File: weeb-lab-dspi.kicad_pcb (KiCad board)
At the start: 2 copper layers, 35.6 x 58.4 mm, 11 parts, among them J1 SPDIF, J2 MONO RCA, U1 XIAO-RP2350-SMD

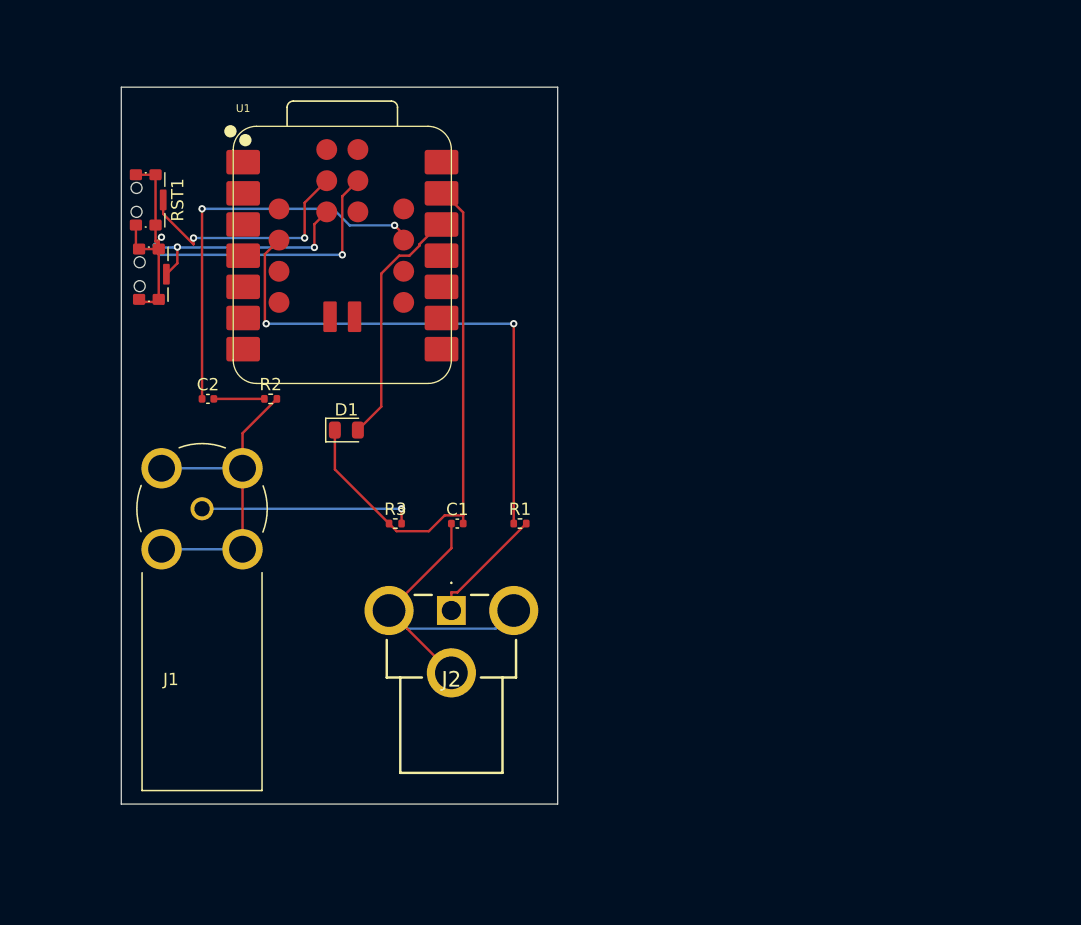
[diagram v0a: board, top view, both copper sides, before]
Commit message: Routed PCB and added more parts
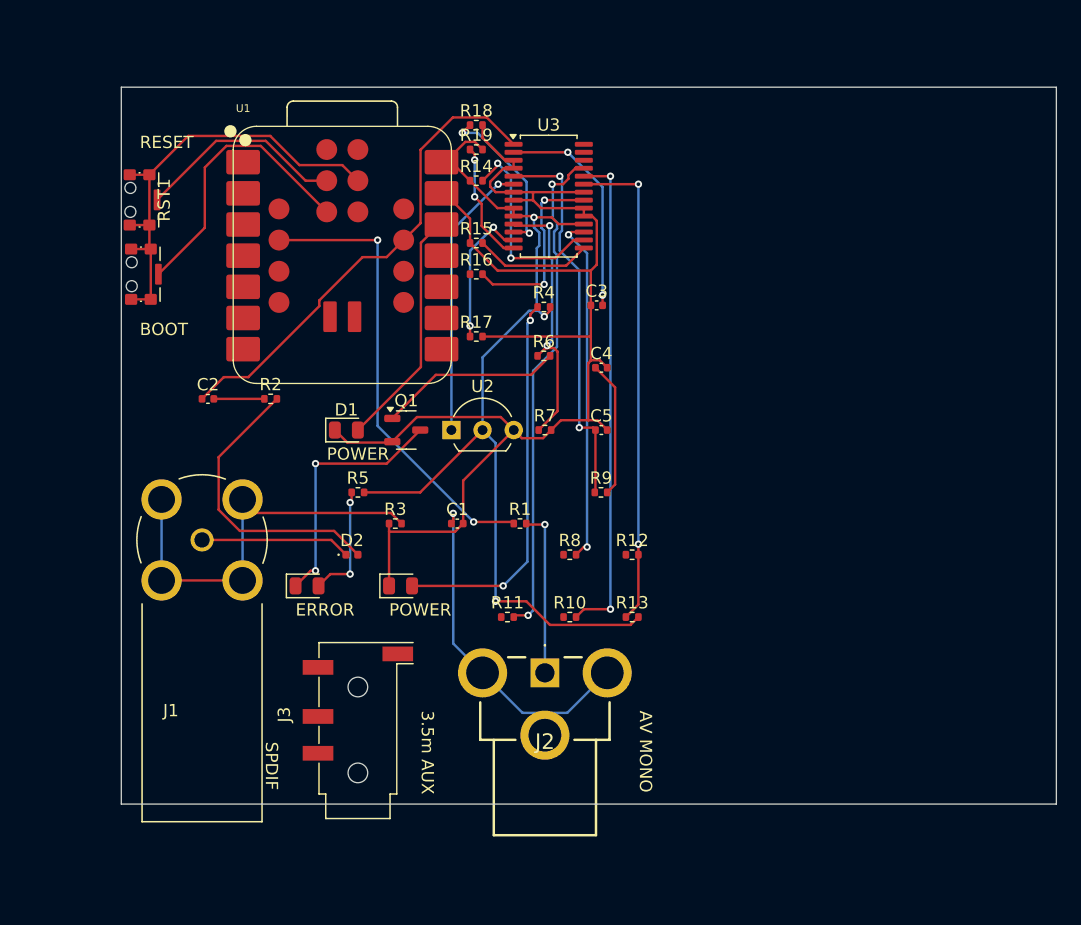
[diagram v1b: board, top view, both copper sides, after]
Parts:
- added C3: 10nf, Capacitor_SMD:C_0402_1005Metric, F.Cu at (176.9, 66.0)
- added C4: 22nf, Capacitor_SMD:C_0402_1005Metric, F.Cu at (177.3, 71.1)
- added C5: 1nf, Capacitor_SMD:C_0402_1005Metric, F.Cu at (177.3, 76.2)
- added D2: BACKFEED_PREVENT, Diode_SMD:D_0402_1005Metric, F.Cu at (157.0, 86.4)
- added D3: POWER, LED_SMD:LED_0805_2012Metric, F.Cu at (161.0, 88.9)
- added D4: ERROR, LED_SMD:LED_0805_2012Metric, F.Cu at (153.3, 88.9)
- added J3: AudioJack3_Ground, Connector_Audio:Jack_3.5mm_KoreanHropartsElec_PJ-320D-4A_Horizontal, F.Cu at (157.5, 99.4)
- added Q1: BC846, Package_TO_SOT_SMD:SOT-23-3, F.Cu at (161.4, 76.2)
- added R10: 33R, Resistor_SMD:R_0402_1005Metric, F.Cu at (174.8, 91.4)
- added R11: 33R, Resistor_SMD:R_0402_1005Metric, F.Cu at (169.7, 91.4)
- added R12: 33R, Resistor_SMD:R_0402_1005Metric, F.Cu at (179.8, 86.4)
- added R13: 47k, Resistor_SMD:R_0402_1005Metric, F.Cu at (179.8, 91.4)
- added R14: 47k, Resistor_SMD:R_0402_1005Metric, F.Cu at (167.1, 55.9)
- added R15: 47k, Resistor_SMD:R_0402_1005Metric, F.Cu at (167.1, 61.0)
- added R16: 33R, Resistor_SMD:R_0402_1005Metric, F.Cu at (167.1, 63.5)
- added R17: 47k, Resistor_SMD:R_0402_1005Metric, F.Cu at (167.1, 68.6)
- added R18: 47k, Resistor_SMD:R_0402_1005Metric, F.Cu at (167.1, 51.4)
- added R19: 47k, Resistor_SMD:R_0402_1005Metric, F.Cu at (167.1, 53.3)
- added R4: 1k2, Resistor_SMD:R_0402_1005Metric, F.Cu at (172.6, 66.2)
- added R5: 1k2, Resistor_SMD:R_0402_1005Metric, F.Cu at (157.5, 81.3)
- added R6: 47k, Resistor_SMD:R_0402_1005Metric, F.Cu at (172.6, 70.2)
- added R7: 47k, Resistor_SMD:R_0402_1005Metric, F.Cu at (172.7, 76.2)
- added R8: 47k, Resistor_SMD:R_0402_1005Metric, F.Cu at (174.8, 86.4)
- added R9: 3k, Resistor_SMD:R_0402_1005Metric, F.Cu at (177.3, 81.3)
- added U2: MCP130-xxxDxTO, Package_TO_SOT_THT:TO-92L_Inline_Wide, F.Cu at (165.1, 76.2)
- added U3: CS8416-xNZ, Package_SO:TSSOP-28_4.4x9.7mm_P0.65mm, F.Cu at (173.0, 57.1)
- moved J2 9.16 mm to (172.7, 96.0)
- moved J1 2.54 mm to (144.8, 85.2)
- moved BOOT1 0.65 mm to (139.8, 63.5)
- moved RST1 0.50 mm to (139.7, 57.4)
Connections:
- net Net-(D1-K) renamed GND
- J1 pad 1: Net-(J1-Pad1) -> Net-(D2-K)
- R2 pad 2: ~ -> Net-(D2-A)
- R3 pad 2: Net-(J1-Pad1) -> ~
- U1 pad 14: unconnected-(U1-5V-Pad14) -> Net-(U1-5V)
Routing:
- net Net-(U1-5V): track 0.00 -> 78.3 mm, vias 0 -> 3
- net GND: track 44.0 -> 112.8 mm
- net Net-(U3-OLRCK): track 0.00 -> 41.0 mm, vias 0 -> 2
- net Net-(U3-OSCLK): track 0.00 -> 40.5 mm, vias 0 -> 2
- net Net-(U3-SDOUT): track 0.00 -> 40.1 mm, vias 0 -> 2
- net Net-(U3-FILT): track 0.00 -> 31.6 mm, vias 0 -> 2
- net Net-(D3-A): track 0.00 -> 31.3 mm, vias 0 -> 2
- net Net-(U3-TX/GPO0): track 0.00 -> 28.6 mm, vias 0 -> 2
- net Net-(D2-A): track 0.00 -> 23.9 mm
- net Net-(U2-~{RST}): track 0.00 -> 22.9 mm, vias 0 -> 1
- net Net-(U3-AD0/~{CS}/NV/RERR): track 0.00 -> 22.3 mm, vias 0 -> 2
- net Net-(D4-K): track 0.00 -> 20.5 mm, vias 0 -> 2
- net Net-(U3-RXN): track 0.00 -> 18.1 mm, vias 0 -> 2
- net Net-(J1-Pad1): track 17.5 -> 0.00 mm, vias 1 -> 0
- net Net-(U3-C/GPO1): track 0.00 -> 16.6 mm, vias 0 -> 2
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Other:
- board size 35.6 x 58.4 mm -> 76.2 x 58.4 mm
- board text added: "3.5m AUX"
- board text added: "AV MONO"
- board text added: "BOOT"
- board text added: "ERROR"
- board text added: "POWER"
- board text added: "RESET"
- board text added: "SPDIF"

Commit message: Almost  Complete
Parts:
- removed J3: AudioJack3_Ground, Connector_Audio:Jack_3.5mm_KoreanHropartsElec_PJ-320D-4A_Horizontal
- added C10: 0.1uf, Capacitor_SMD:C_0402_1005Metric, F.Cu at (165.5, 99.1)
- added C11: 0.1uf, Capacitor_SMD:C_0402_1005Metric, F.Cu at (170.6, 99.1)
- added C12: 10uf, Capacitor_SMD:C_0402_1005Metric, F.Cu at (163.0, 99.1)
- added C13: 10uf, Capacitor_SMD:C_0402_1005Metric, F.Cu at (163.0, 101.0)
- added C6: 10uf, Capacitor_SMD:C_0402_1005Metric, F.Cu at (177.8, 83.8)
- added C7: 10uf, Capacitor_SMD:C_0402_1005Metric, F.Cu at (144.8, 68.6)
- added C8: 10uf, Capacitor_SMD:C_0402_1005Metric, F.Cu at (175.3, 83.8)
- added C9: 10uf, Capacitor_SMD:C_0402_1005Metric, F.Cu at (144.8, 66.0)
- added D5: BACKFEED_PREVENT, Diode_SMD:D_0402_1005Metric, F.Cu at (174.8, 53.3)
- added J4: AudioJack3_Ground, Connector_Audio:Jack_3.5mm_CUI_SJ-3524-SMT_Horizontal, F.Cu at (156.7, 103.6)
- added LEFT1: TPA6203A1DRB, Package_DFN_QFN:Texas_DRB0008A, F.Cu at (166.6, 103.2)
- added RIGHT1: TPA6203A1DRB, Package_DFN_QFN:Texas_DRB0008A, F.Cu at (171.4, 103.2)
- added U4: CS434x-xZZ, Package_SO:TSSOP-10_3x3mm_P0.5mm, F.Cu at (167.6, 96.5)
- moved R7 18.5 mm to (177.8, 58.4)
- moved U2 18.5 mm to (170.2, 58.4)
- moved R10 10.2 mm to (174.8, 81.3)
- moved U3 9.85 mm to (182.9, 57.1)
- moved J2 8.03 mm to (180.3, 98.5)
- moved R2 5.08 mm to (145.3, 73.7)
- moved C2 5.08 mm to (145.3, 78.7)
- moved J1 5.08 mm to (144.8, 90.2)
- moved R13 3.59 mm to (177.3, 88.9)
- moved R18 3.23 mm to (169.7, 53.3)
- moved D4 2.54 mm to (153.3, 86.4)
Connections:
- C2 pad 1: Net-(U1-GPIO20/D12/TX1) -> Net-(D5-A)
- R10 pad 1: unconnected-(R10-Pad1) -> Net-(U4-~{DEM}/SCLK)
- R11 pad 1: unconnected-(R11-Pad1) -> Net-(U4-LRCK)
- R12 pad 1: unconnected-(R12-Pad1) -> Net-(U4-SDIN)
- R16 pad 1: unconnected-(R16-Pad1) -> Net-(U4-MCLK)
- U1 pad 16: Net-(U1-GPIO20/D12/TX1) -> Net-(D5-A)
- U3 pad 1: Net-(U1-GPIO20/D12/TX1) -> Net-(D5-K)
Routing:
- net GND: track 112.8 -> 222.5 mm, vias 0 -> 3
- net Net-(D5-A): track 0.00 -> 68.1 mm
- net Net-(RIGHT1-IN+): track 0.00 -> 64.1 mm, vias 0 -> 2
- net Net-(U4-AOUTR): track 0.00 -> 58.1 mm, vias 0 -> 2
- net Net-(U4-MCLK): track 0.00 -> 47.8 mm, vias 0 -> 4
- net Net-(U4-VQ): track 0.00 -> 41.0 mm
- net Net-(U1-GPIO20/D12/TX1): track 39.6 -> 0.00 mm
- net Net-(U4-FILT+): track 0.00 -> 20.9 mm, vias 0 -> 2
- net Net-(U4-SDIN): track 0.00 -> 20.0 mm, vias 0 -> 2
- net Net-(U4-~{DEM}/SCLK): track 0.00 -> 18.9 mm
- net Net-(J2-Pad1): track 13.6 -> 31.5 mm
- net Net-(U4-AOUTL): track 0.00 -> 17.2 mm
- net Net-(U3-OLRCK): track 41.0 -> 58.1 mm
- net Net-(RIGHT1-V_{O+}): track 0.00 -> 16.1 mm, vias 0 -> 2
- net Net-(C13-Pad2): track 0.00 -> 13.2 mm
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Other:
- board size 76.2 x 58.4 mm -> 50.8 x 58.4 mm

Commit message: Finally
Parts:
- removed D1: POWER, LED_SMD:LED_0805_2012Metric
- moved BOOT1 7.61 mm to (132.2, 63.5)
- moved RST1 7.61 mm to (132.1, 57.4)
- moved C10 5.17 mm to (170.7, 99.1)
- moved C11 4.99 mm to (165.6, 99.1)
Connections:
- LEFT1 pad 6: GND -> Net-(LEFT1-V_{DD})
- RIGHT1 pad 6: GND -> Net-(LEFT1-V_{DD})
- U1 pad 12: Net-(D1-A) -> Net-(LEFT1-V_{DD})
- U3 pad 20: GND -> Net-(LEFT1-V_{DD})
- U3 pad 3: GND -> Net-(LEFT1-V_{DD})
- U4 pad 9: GND -> Net-(LEFT1-V_{DD})
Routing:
- net Net-(LEFT1-V_{DD}): track 0.00 -> 111.7 mm, vias 0 -> 4
- net Net-(LEFT1-IN+): track 0.00 -> 32.8 mm, vias 0 -> 2
- net Net-(D1-A): track 20.1 -> 0.00 mm
- net Net-(D5-A): track 68.1 -> 54.7 mm, vias 0 -> 2
- net Net-(Q1-B): track 28.0 -> 15.0 mm, vias 2 -> 0
- net Net-(U4-MCLK): track 47.8 -> 36.3 mm, vias 4 -> 2
- net Net-(U4-AOUTR): track 58.1 -> 48.3 mm
- net Net-(U3-AD1/CDIN/~{AUDIO}): track 14.5 -> 23.3 mm, vias 0 -> 2
- net Net-(U1-5V): track 86.7 -> 95.4 mm, vias 6 -> 4
- net Net-(J2-Pad1): track 31.5 -> 22.8 mm
- net Net-(RST1-B): track 17.5 -> 24.8 mm
- net Net-(U1-GND_1): track 37.1 -> 44.0 mm
- net Net-(RIGHT1-V_{O+}): track 16.1 -> 22.9 mm
- net Net-(LEFT1-BYPASS): track 11.1 -> 4.43 mm
- net Net-(BOOT1-B): track 24.2 -> 30.8 mm
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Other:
- board size 50.8 x 58.4 mm -> 66 x 66 mm

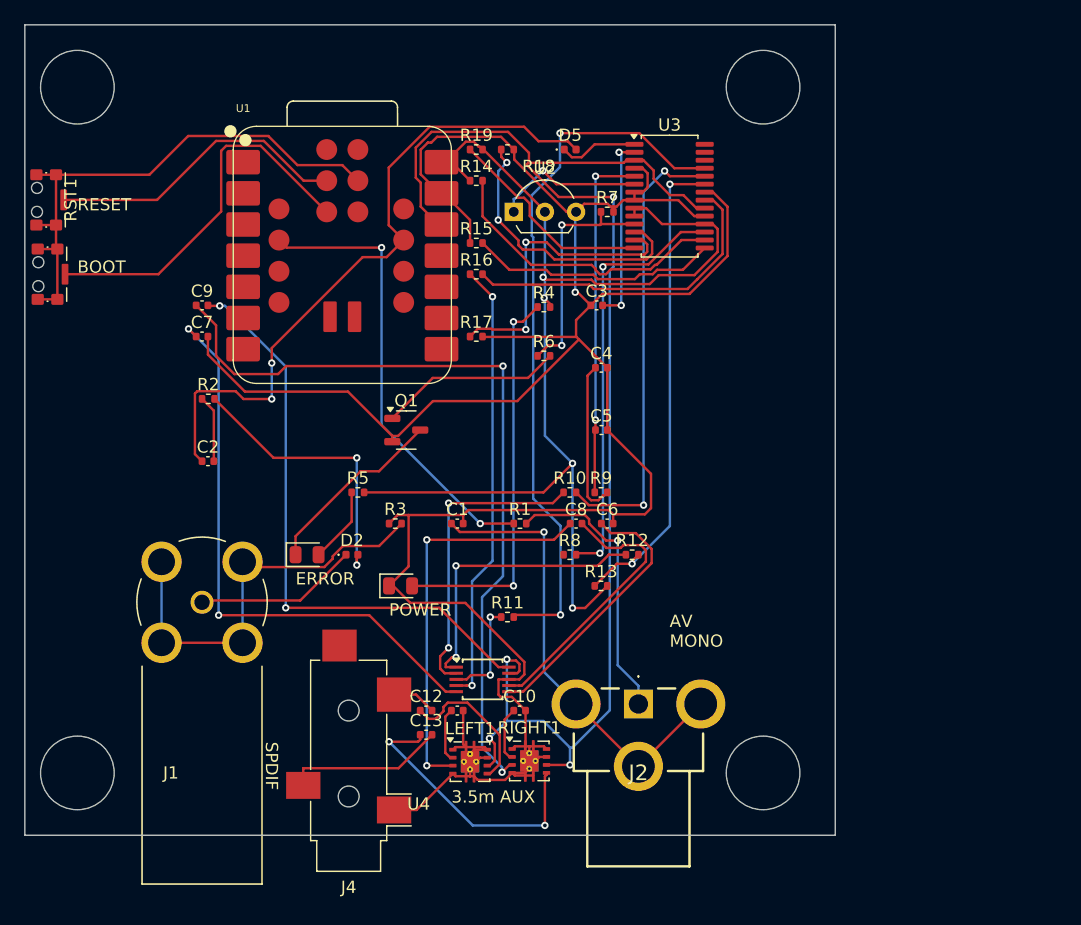
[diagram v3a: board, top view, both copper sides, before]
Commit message: Add power bypass caps
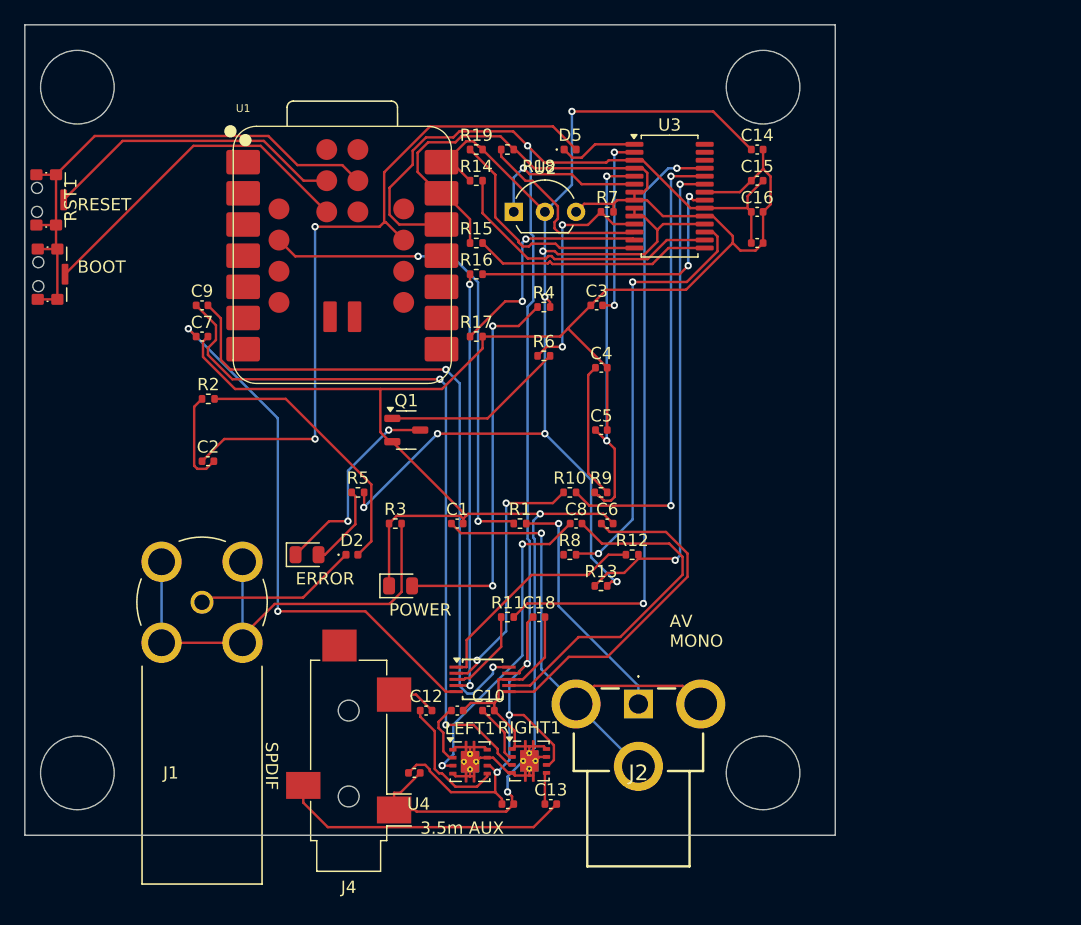
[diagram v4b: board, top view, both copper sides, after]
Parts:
- added C14: 100nf, Capacitor_SMD:C_0402_1005Metric, F.Cu at (190.0, 53.3)
- added C15: 100nf, Capacitor_SMD:C_0402_1005Metric, F.Cu at (190.0, 55.9)
- added C16: 100nf, Capacitor_SMD:C_0402_1005Metric, F.Cu at (190.0, 58.4)
- added C17: 1nf, Capacitor_SMD:C_0402_1005Metric, F.Cu at (190.0, 61.0)
- added C18: 100nf, Capacitor_SMD:C_0402_1005Metric, F.Cu at (172.2, 91.4)
- added C19: 100nf, Capacitor_SMD:C_0402_1005Metric, F.Cu at (169.7, 106.7)
- added C20: 100nf, Capacitor_SMD:C_0402_1005Metric, F.Cu at (162.1, 104.1)
- moved C13 11.6 mm to (173.2, 106.7)
- moved C10 2.54 mm to (168.1, 99.1)
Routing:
- net Net-(RIGHT1-V_{O+}): track 22.9 -> 2.59 mm, vias 2 -> 0
- net GND: track 222.3 -> 241.7 mm, vias 1 -> 2
- net Net-(U1-5V): track 95.4 -> 110.0 mm, vias 4 -> 7
- net Net-(LEFT1-V_{DD}): track 111.7 -> 124.4 mm
- net Net-(C13-Pad2): track 13.0 -> 23.7 mm
- net Net-(U3-AD1/CDIN/~{AUDIO}): track 23.3 -> 15.5 mm, vias 2 -> 0
- net Net-(U3-OLRCK): track 58.0 -> 50.3 mm
- net Net-(U4-AOUTR): track 48.3 -> 55.3 mm
- net Net-(LEFT1-IN+): track 32.8 -> 26.2 mm
- net Net-(U4-FILT+): track 22.1 -> 28.4 mm
- net Net-(U4-AOUTL): track 22.6 -> 28.7 mm
- net ~: track 34.5 -> 40.4 mm
- net Net-(U4-SDIN): track 23.9 -> 18.9 mm, vias 2 -> 0
- net Net-(RIGHT1-IN+): track 64.6 -> 60.0 mm
- net Net-(U3-SCL/CCLK/96KHZ): track 24.1 -> 19.6 mm
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
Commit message: Adding Labeling
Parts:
- moved C17 14.8 mm to (177.3, 53.3)
- moved C14 7.62 mm to (190.0, 61.0)
- moved C15 2.54 mm to (190.0, 53.3)
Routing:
- net GND: track 241.7 -> 274.3 mm, vias 2 -> 1
- net Net-(LEFT1-V_{DD}): track 124.4 -> 144.2 mm, vias 4 -> 5
- net Net-(U1-5V): track 110.0 -> 94.3 mm, vias 7 -> 3
- net Net-(U4-AOUTL): track 28.7 -> 17.2 mm, vias 0 -> 2
- net Net-(U4-FILT+): track 28.4 -> 19.2 mm, vias 0 -> 2
- net Net-(U4-~{DEM}/SCLK): track 21.1 -> 27.2 mm, vias 2 -> 0
- net Net-(U4-VQ): track 44.2 -> 49.7 mm
- net Net-(U4-AOUTR): track 55.3 -> 50.0 mm, vias 2 -> 4
- net Net-(U3-C/GPO1): track 23.1 -> 27.8 mm, vias 0 -> 2
- net Net-(C1-Pad1): track 41.3 -> 36.7 mm
- net Net-(U3-RXN): track 15.1 -> 19.3 mm
- net ~: track 40.4 -> 36.8 mm
- net Net-(U3-FILT): track 32.0 -> 28.5 mm
- net Net-(LEFT1-IN+): track 26.2 -> 29.2 mm
- net Net-(C2-Pad2): track 7.68 -> 5.48 mm
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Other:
- board text added: "2026 version 1.0"
- board text added: "2026 バージョン 1.0"
- board text added: "AUX端子"
- board text added: "AV MONO OUT"
- board text added: "AV モノラル出力"
- board text added: "Aux"
- board text added: "Board by: @darrenwjlau ボード作成者: @darrenwjlau"
- board text added: "Credits クレジット"
- board text added: "Outputs: Mono AV Out Coax SPDIF Stereo 3.5"
- board text added: "Powered by: WeebLab's DSPI 提供： WeebLab の DSPI"
- board text added: "USB C (Audio Input)"
- board text added: "USBタイプC （オーディオ入力）"
- board text added: "WeebDSP"
- board text added: "ウィーブDSP"
- board text added: "エスピーディーアイエフ"
- board text added: "エラー"
- board text added: "ブート"
- board text added: "リセット"
- board text added: "出力： モノラルAV出力 同軸SPDIF ステレオ3.5"
- board text added: "電源"
- board text removed: "3.5m AUX"
- board text removed: "AV MONO"
